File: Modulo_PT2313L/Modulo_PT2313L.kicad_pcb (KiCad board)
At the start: 2 copper layers, 100 x 50 mm, 40 parts, among them J1 Power 9V, J2 LF_Amp, J3 RF_Amp, J4 LR_Amp, J5 RR_Amp, J6 I2C_Conn, J7 Inputs, U1 PT2313

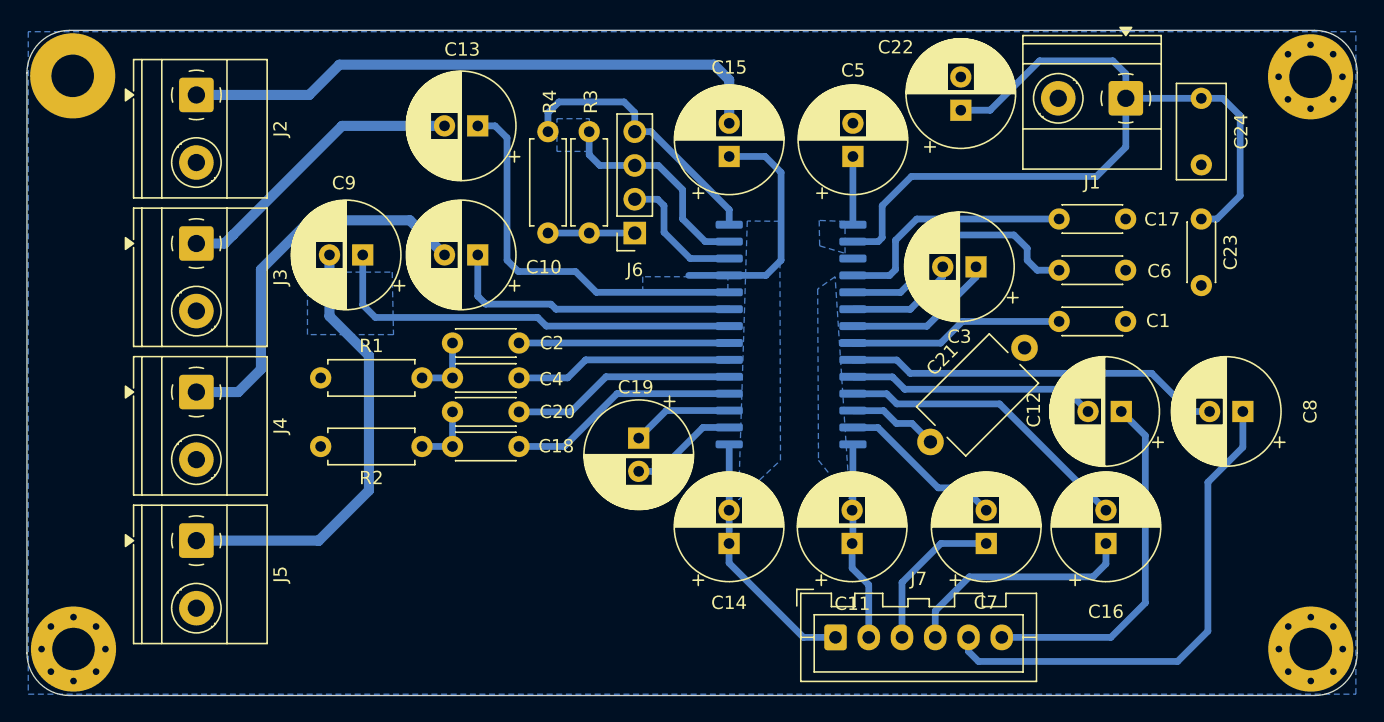
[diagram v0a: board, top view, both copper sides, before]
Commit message: Cambios en la Serigrafia
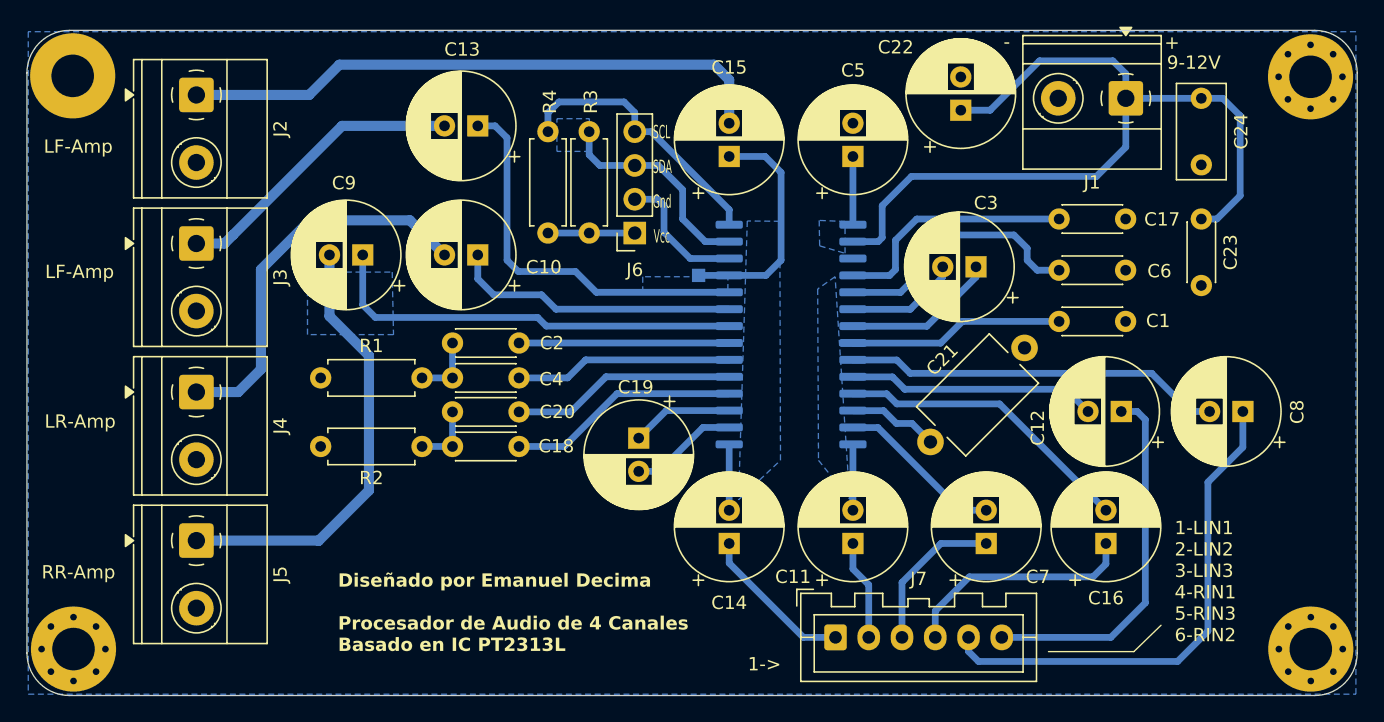
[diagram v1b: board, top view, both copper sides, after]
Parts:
- added REF**: TestPoint_Pad_1.0x1.0mm, TestPoint:TestPoint_Pad_1.0x1.0mm, B.Cu at (130.0, 58.7)
- moved C11 0.06 mm to (141.6, 78.9)
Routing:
- net Net-(U1-LIN2): track 6.60 -> 4.95 mm
- net Net-(U1-LIN1): track 6.60 -> 4.95 mm
- net Net-(U1-LROUT): track 22.4 -> 21.6 mm
- net Net-(U1-LFOUT): track 18.4 -> 17.7 mm
- net /RIN2: track 27.0 -> 27.7 mm
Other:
- board text added: "+"
- board text added: "-"
- board text added: "1->"
- board text added: "1-LIN1 2-LIN2 3-LIN3 4-RIN1 5-RIN3 6-RIN2"
- board text added: "9-12V"
- board text added: "Diseñado por Emanuel Decima Procesador de Audio de 4 Canales Basado en IC PT2313L"
- board text added: "Gnd"
- board text added: "LF-Amp"
- board text added: "LR-Amp"
- board text added: "RR-Amp"
- board text added: "SCL"
- board text added: "SDA"
- board text added: "Vcc"
